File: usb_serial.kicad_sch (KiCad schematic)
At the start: 13 parts, among them J52 USB_B_Micro, J53 Conn_02x04_Odd_Even, Q8 S8050, Q9 S8050, U27 CH340C

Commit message: WIP v0.2.0 changes
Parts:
- renumbered J52 to J46, J53 to J47
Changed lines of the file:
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@@
+		(polyline
+			(pts
+				(xy 107.95 67.31) (xy 107.95 72.39) (xy 105.41 72.39) (xy 105.41 67.31)
+			)
+			(stroke
+				(width 0)
+				(type dash)
+			)
+			(fill
+				(type none)
+			)
+		)
+	)
+	(rule_area
 		(polyline
 			(pts
 				(xy 72.39 74.93) (xy 69.85 74.93) (xy 69.85 80.01) (xy 72.39 80.01)
-			)
-			(stroke
-				(width 0)
-				(type dash)
-			)
-			(fill
-				(type none)
-			)
-		)
-	)
-	(rule_area
-		(polyline
-			(pts
-				(xy 107.95 67.31) (xy 107.95 72.39) (xy 105.41 72.39) (xy 105.41 67.31)
 			)
 			(stroke
@@
 		(on_board yes)
 		(dnp no)
-		(property "Reference" "J52"
+		(property "Reference" "J46"
 			(at 54.7878 64.3382 0)
 			(effects
@@
 			(project "HALSPA"
 				(path "/7eeba806-440e-4671-bc07-69fe183910a7/d2563b9c-21b7-43a8-ad57-d0568fac8495"
-					(reference "J52")
+					(reference "J46")
 					(unit 1)
 				)
@@
 		(on_board yes)
 		(dnp no)
-		(property "Reference" "#PWR0211"
+		(property "Reference" "#PWR0206"
 			(at 190.5 72.39 0)
 			(effects
@@
 			(project "HALSPA"
 				(path "/7eeba806-440e-4671-bc07-69fe183910a7/d2563b9c-21b7-43a8-ad57-d0568fac8495"
-					(reference "#PWR0211")
+					(reference "#PWR0206")
 					(unit 1)
 				)
@@
 		(dnp no)
 		(fields_autoplaced yes)
-		(property "Reference" "J53"
+		(property "Reference" "J47"
 			(at 240.03 68.58 0)
 			(effects
@@
 			(project ""
 				(path "/7eeba806-440e-4671-bc07-69fe183910a7/d2563b9c-21b7-43a8-ad57-d0568fac8495"
-					(reference "J53")
+					(reference "J47")
 					(unit 1)
 				)
@@
 		(on_board yes)
 		(dnp no)
-		(property "Reference" "#PWR0212"
+		(property "Reference" "#PWR0207"
 			(at 229.87 74.93 0)
 			(effects
@@
 			(project "HALSPA"
 				(path "/7eeba806-440e-4671-bc07-69fe183910a7/d2563b9c-21b7-43a8-ad57-d0568fac8495"
-					(reference "#PWR0212")
+					(reference "#PWR0207")
 					(unit 1)
 				)
@@
 		(on_board yes)
 		(dnp no)
-		(property "Reference" "#PWR0208"
+		(property "Reference" "#PWR0203"
 			(at 105.41 60.96 0)
 			(effects
@@
 			(project "HALSPA"
 				(path "/7eeba806-440e-4671-bc07-69fe183910a7/d2563b9c-21b7-43a8-ad57-d0568fac8495"
-					(reference "#PWR0208")
+					(reference "#PWR0203")
 					(unit 1)
 				)
@@
 		(dnp no)
 		(fields_autoplaced yes)
-		(property "Reference" "#PWR0210"
+		(property "Reference" "#PWR0205"
 			(at 190.5 52.07 0)
 			(effects
@@
 			(project "HALSPA"
 				(path "/7eeba806-440e-4671-bc07-69fe183910a7/d2563b9c-21b7-43a8-ad57-d0568fac8495"
-					(reference "#PWR0210")
+					(reference "#PWR0205")
 					(unit 1)
 				)
@@
 		(on_board yes)
 		(dnp no)
-		(property "Reference" "#PWR0207"
+		(property "Reference" "#PWR0202"
 			(at 93.98 100.33 0)
 			(effects
@@
 			(project "HALSPA"
 				(path "/7eeba806-440e-4671-bc07-69fe183910a7/d2563b9c-21b7-43a8-ad57-d0568fac8495"
-					(reference "#PWR0207")
+					(reference "#PWR0202")
 					(unit 1)
 				)
@@
 		(on_board yes)
 		(dnp no)
-		(property "Reference" "#PWR0205"
+		(property "Reference" "#PWR0200"
 			(at 53.34 99.06 0)
 			(effects
@@
 			(project "HALSPA"
 				(path "/7eeba806-440e-4671-bc07-69fe183910a7/d2563b9c-21b7-43a8-ad57-d0568fac8495"
-					(reference "#PWR0205")
+					(reference "#PWR0200")
 					(unit 1)
 				)
@@
 		(on_board yes)
 		(dnp no)
-		(property "Reference" "#PWR0213"
+		(property "Reference" "#PWR0208"
 			(at 246.38 88.9 0)
 			(effects
@@
 			(project "HALSPA"
 				(path "/7eeba806-440e-4671-bc07-69fe183910a7/d2563b9c-21b7-43a8-ad57-d0568fac8495"
-					(reference "#PWR0213")
+					(reference "#PWR0208")
 					(unit 1)
 				)
@@
 		(dnp no)
 		(fields_autoplaced yes)
-		(property "Reference" "#PWR0209"
+		(property "Reference" "#PWR0204"
 			(at 186.69 92.71 0)
 			(effects
@@
 			(project "HALSPA"
 				(path "/7eeba806-440e-4671-bc07-69fe183910a7/d2563b9c-21b7-43a8-ad57-d0568fac8495"
-					(reference "#PWR0209")
+					(reference "#PWR0204")
 					(unit 1)
 				)
@@
 		(dnp no)
 		(fields_autoplaced yes)
-		(property "Reference" "#PWR0206"
+		(property "Reference" "#PWR0201"
 			(at 91.44 54.61 0)
 			(effects
@@
 			(project ""
 				(path "/7eeba806-440e-4671-bc07-69fe183910a7/d2563b9c-21b7-43a8-ad57-d0568fac8495"
-					(reference "#PWR0206")
-					(unit 1)
-				)
+					(reference "#PWR0201")
+					(unit 1)
+				)

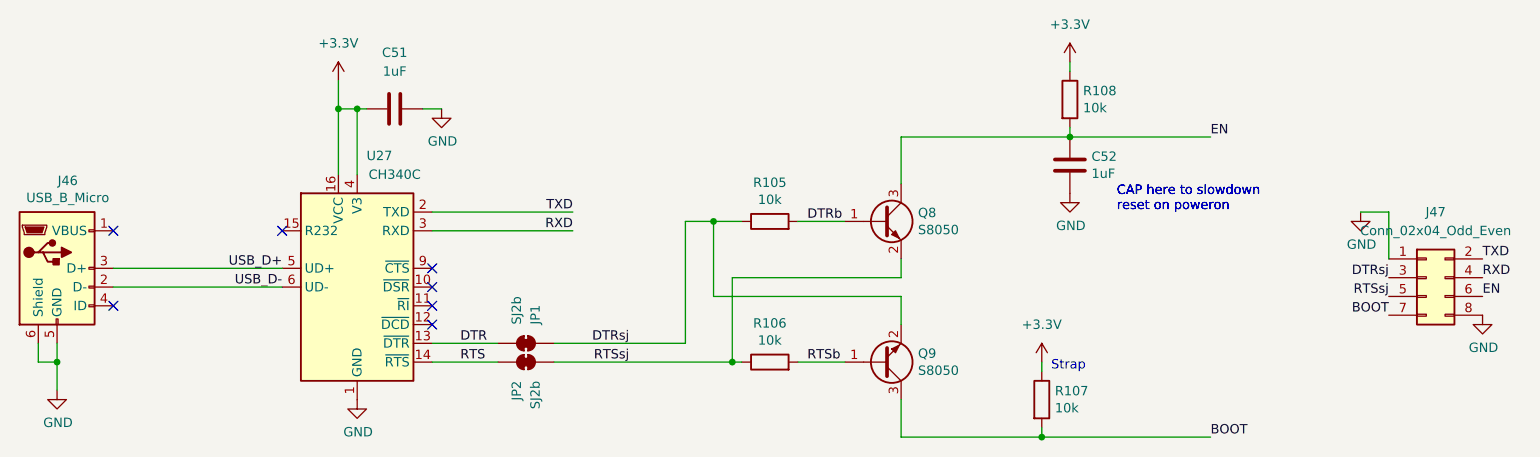
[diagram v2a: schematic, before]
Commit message: Assign part numbers and finish other 0.2.0 changes
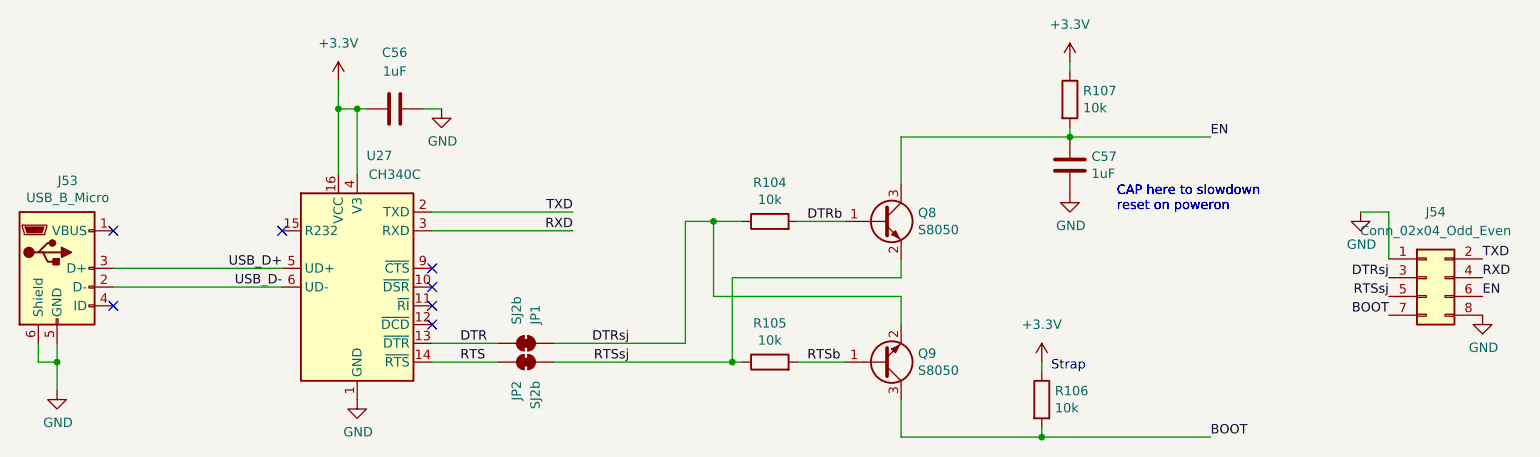
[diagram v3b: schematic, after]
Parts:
- J54: renamed from J47; LCSC (none) -> C7501275
- renumbered C51 to C56, C52 to C57, J46 to J53, R105 to R104, R106 to R105, R107 to R106, R108 to R107
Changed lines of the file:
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@@
 		(on_board yes)
 		(dnp no)
-		(property "Reference" "J46"
+		(property "Reference" "J53"
 			(at 54.7878 64.3382 0)
 			(effects
@@
 			(project "HALSPA"
 				(path "/7eeba806-440e-4671-bc07-69fe183910a7/d2563b9c-21b7-43a8-ad57-d0568fac8495"
-					(reference "J46")
+					(reference "J53")
 					(unit 1)
 				)
@@
 		(on_board yes)
 		(dnp no)
-		(property "Reference" "R106"
+		(property "Reference" "R105"
 			(at 149.86 83.6422 90)
 			(effects
@@
 			(project "HALSPA"
 				(path "/7eeba806-440e-4671-bc07-69fe183910a7/d2563b9c-21b7-43a8-ad57-d0568fac8495"
-					(reference "R106")
+					(reference "R105")
 					(unit 1)
 				)
@@
 		(on_board yes)
 		(dnp no)
-		(property "Reference" "#PWR0206"
+		(property "Reference" "#PWR0216"
 			(at 190.5 72.39 0)
 			(effects
@@
 			(project "HALSPA"
 				(path "/7eeba806-440e-4671-bc07-69fe183910a7/d2563b9c-21b7-43a8-ad57-d0568fac8495"
-					(reference "#PWR0206")
+					(reference "#PWR0216")
 					(unit 1)
 				)
@@
 		(on_board yes)
 		(dnp no)
-		(property "Reference" "R107"
+		(property "Reference" "R106"
 			(at 188.468 92.8116 0)
 			(effects
@@
 			(project "HALSPA"
 				(path "/7eeba806-440e-4671-bc07-69fe183910a7/d2563b9c-21b7-43a8-ad57-d0568fac8495"
-					(reference "R107")
+					(reference "R106")
 					(unit 1)
 				)
@@
 		(on_board yes)
 		(dnp no)
-		(property "Reference" "C52"
+		(property "Reference" "C57"
 			(at 193.421 61.0616 0)
 			(effects
@@
 			(project "HALSPA"
 				(path "/7eeba806-440e-4671-bc07-69fe183910a7/d2563b9c-21b7-43a8-ad57-d0568fac8495"
-					(reference "C52")
+					(reference "C57")
 					(unit 1)
 				)
@@
 		(dnp no)
 		(fields_autoplaced yes)
-		(property "Reference" "J47"
+		(property "Reference" "J54"
 			(at 240.03 68.58 0)
 			(effects
@@
 			)
 		)
+		(property "LCSC" "C7501275"
+			(at 238.76 77.47 0)
+			(effects
+				(font
+					(size 1.27 1.27)
+				)
+				(hide yes)
+			)
+		)
 		(pin "1"
 		)
@@
 			(project ""
 				(path "/7eeba806-440e-4671-bc07-69fe183910a7/d2563b9c-21b7-43a8-ad57-d0568fac8495"
-					(reference "J47")
+					(reference "J54")
 					(unit 1)
 				)
@@
 		(on_board yes)
 		(dnp no)
-		(property "Reference" "#PWR0207"
+		(property "Reference" "#PWR0217"
 			(at 229.87 74.93 0)
 			(effects
@@
 			(project "HALSPA"
 				(path "/7eeba806-440e-4671-bc07-69fe183910a7/d2563b9c-21b7-43a8-ad57-d0568fac8495"
-					(reference "#PWR0207")
+					(reference "#PWR0217")
 					(unit 1)
 				)
@@
 		(on_board yes)
 		(dnp no)
-		(property "Reference" "R108"
+		(property "Reference" "R107"
 			(at 192.278 52.1716 0)
 			(effects
@@
 			(project "HALSPA"
 				(path "/7eeba806-440e-4671-bc07-69fe183910a7/d2563b9c-21b7-43a8-ad57-d0568fac8495"
-					(reference "R108")
+					(reference "R107")
 					(unit 1)
 				)
@@
 		(on_board yes)
 		(dnp no)
-		(property "Reference" "R105"
+		(property "Reference" "R104"
 			(at 149.86 64.5922 90)
 			(effects
@@
 			(project "HALSPA"
 				(path "/7eeba806-440e-4671-bc07-69fe183910a7/d2563b9c-21b7-43a8-ad57-d0568fac8495"
-					(reference "R105")
+					(reference "R104")
 					(unit 1)
 				)
@@
 		(on_board yes)
 		(dnp no)
-		(property "Reference" "#PWR0203"
+		(property "Reference" "#PWR0213"
 			(at 105.41 60.96 0)
 			(effects
@@
 			(project "HALSPA"
 				(path "/7eeba806-440e-4671-bc07-69fe183910a7/d2563b9c-21b7-43a8-ad57-d0568fac8495"
-					(reference "#PWR0203")
+					(reference "#PWR0213")
 					(unit 1)
 				)
@@
 		(dnp no)
 		(fields_autoplaced yes)
-		(property "Reference" "#PWR0205"
+		(property "Reference" "#PWR0215"
 			(at 190.5 52.07 0)
 			(effects
@@
 			(project "HALSPA"
 				(path "/7eeba806-440e-4671-bc07-69fe183910a7/d2563b9c-21b7-43a8-ad57-d0568fac8495"
-					(reference "#PWR0205")
+					(reference "#PWR0215")
 					(unit 1)
 				)
@@
 		(on_board yes)
 		(dnp no)
-		(property "Reference" "#PWR0202"
+		(property "Reference" "#PWR0212"
 			(at 93.98 100.33 0)
 			(effects
@@
 			(project "HALSPA"
 				(path "/7eeba806-440e-4671-bc07-69fe183910a7/d2563b9c-21b7-43a8-ad57-d0568fac8495"
-					(reference "#PWR0202")
+					(reference "#PWR0212")
 					(unit 1)
 				)
@@
 		(on_board yes)
 		(dnp no)
-		(property "Reference" "#PWR0200"
+		(property "Reference" "#PWR0210"
 			(at 53.34 99.06 0)
 			(effects
@@
 			(project "HALSPA"
 				(path "/7eeba806-440e-4671-bc07-69fe183910a7/d2563b9c-21b7-43a8-ad57-d0568fac8495"
-					(reference "#PWR0200")
+					(reference "#PWR0210")
 					(unit 1)
 				)
@@
 		(on_board yes)
 		(dnp no)
-		(property "Reference" "#PWR0208"
+		(property "Reference" "#PWR0218"
 			(at 246.38 88.9 0)
 			(effects
@@
 			(project "HALSPA"
 				(path "/7eeba806-440e-4671-bc07-69fe183910a7/d2563b9c-21b7-43a8-ad57-d0568fac8495"
-					(reference "#PWR0208")
+					(reference "#PWR0218")
 					(unit 1)
 				)
@@
 		(dnp no)
 		(fields_autoplaced yes)
-		(property "Reference" "C51"
+		(property "Reference" "C56"
 			(at 99.06 46.99 90)
 			(effects
@@
 			(project "HALSPA"
 				(path "/7eeba806-440e-4671-bc07-69fe183910a7/d2563b9c-21b7-43a8-ad57-d0568fac8495"
-					(reference "C51")
+					(reference "C56")
 					(unit 1)
 				)
@@
 		(dnp no)
 		(fields_autoplaced yes)
-		(property "Reference" "#PWR0204"
+		(property "Reference" "#PWR0214"
 			(at 186.69 92.71 0)
 			(effects
@@
 			(project "HALSPA"
 				(path "/7eeba806-440e-4671-bc07-69fe183910a7/d2563b9c-21b7-43a8-ad57-d0568fac8495"
-					(reference "#PWR0204")
+					(reference "#PWR0214")
 					(unit 1)
 				)
@@
 		(dnp no)
 		(fields_autoplaced yes)
-		(property "Reference" "#PWR0201"
+		(property "Reference" "#PWR0211"
 			(at 91.44 54.61 0)
 			(effects
@@
 			(project ""
 				(path "/7eeba806-440e-4671-bc07-69fe183910a7/d2563b9c-21b7-43a8-ad57-d0568fac8495"
-					(reference "#PWR0201")
-					(unit 1)
-				)
+					(reference "#PWR0211")
+					(unit 1)
+				)

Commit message: Update the title blocks
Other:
- company: (none) -> Hat Labs Oy
- title: (none) -> HALSPA - Hat Labs Spaghetti Board
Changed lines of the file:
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@@
 	(generator_version "9.0")
 	(paper "A4")
+	(title_block
+		(title "HALSPA - Hat Labs Spaghetti Board")
+		(date "2025-04-17")
+		(rev "v0.2.0")
+		(company "Hat Labs Oy")
+		(comment 1 "See the accompanying LICENSE.md file for license details.")
+	)
 	(text "CAP here to slowdown \nreset on poweron"
 		(exclude_from_sim no)
@@
 		(polyline
 			(pts
-				(xy 107.95 67.31) (xy 107.95 72.39) (xy 105.41 72.39) (xy 105.41 67.31)
-			)
-			(stroke
-				(width 0)
-				(type dash)
-			)
-			(fill
-				(type none)
-			)
-		)
-	)
-	(rule_area
-		(polyline
-			(pts
 				(xy 72.39 74.93) (xy 69.85 74.93) (xy 69.85 80.01) (xy 72.39 80.01)
 			)
@@
 			)
 			(stroke
+				(width 0)
+				(type dash)
+			)
+			(fill
+				(type none)
+			)
+		)
+	)
+	(rule_area
+		(polyline
+			(pts
+				(xy 107.95 67.31) (xy 107.95 72.39) (xy 105.41 72.39) (xy 105.41 67.31)
+			)
+			(stroke

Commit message: Add JLCPCB corrections
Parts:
- J53: JLCPCB_CORRECTION 1.3;0.5;0 -> (none)
- J54: JLCPCB_CORRECTION (none) -> 1.27;3.81;270
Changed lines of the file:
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@@
+		(polyline
+			(pts
+				(xy 107.95 67.31) (xy 107.95 72.39) (xy 105.41 72.39) (xy 105.41 67.31)
+			)
+			(stroke
+				(width 0)
+				(type dash)
+			)
+			(fill
+				(type none)
+			)
+		)
+	)
+	(rule_area
 		(polyline
 			(pts
 				(xy 139.7 52.07) (xy 181.61 52.07) (xy 181.61 102.87) (xy 139.7 102.87)
-			)
-			(stroke
-				(width 0)
-				(type dash)
-			)
-			(fill
-				(type none)
-			)
-		)
-	)
-	(rule_area
-		(polyline
-			(pts
-				(xy 107.95 67.31) (xy 107.95 72.39) (xy 105.41 72.39) (xy 105.41 67.31)
 			)
 			(stroke
@@
 			)
 		)
-		(property "JLCPCB_CORRECTION" "1.3;0.5;0"
+		(property "JLCPCB_CORRECTION" ""
 			(at 53.34 76.2 0)
 			(effects
@@
 			(at 238.76 77.47 0)
 			(effects
+				(font
+					(size 1.27 1.27)
+				)
+				(hide yes)
+			)
+		)
+		(property "JLCPCB_CORRECTION" "1.27;3.81;270"
+			(at 238.76 77.47 0)
+			(effects
